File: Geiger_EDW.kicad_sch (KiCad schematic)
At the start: 44 parts, among them J1 Power, J2 +5V Output, J3 STS-5, J4 Piezo, J5 Output, P1 500k, Q1 IRF7404, Q2 BC857, Q3 IRFBC40SPBF, Q4 BC847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

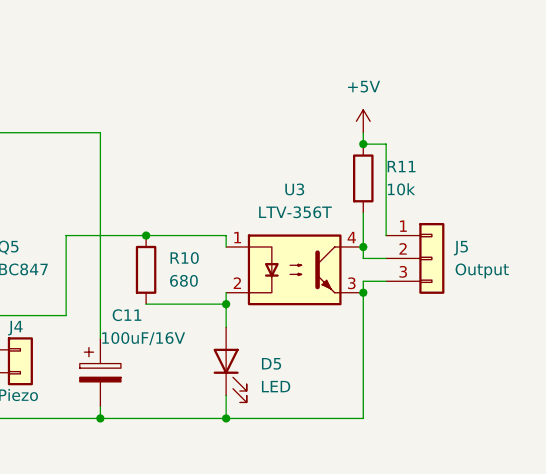
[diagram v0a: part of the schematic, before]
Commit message: Change R11 value from 10k to 1k
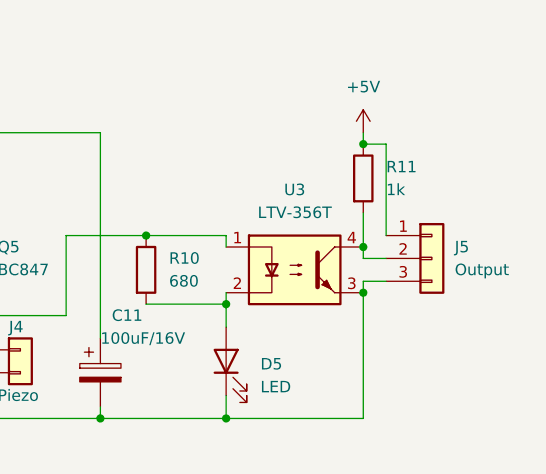
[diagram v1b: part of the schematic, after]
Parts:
- R11: value 10k -> 1k
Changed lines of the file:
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@@
       (effects (font (size 1.27 1.27)) (justify left))
     )
-    (property "Value" "10k" (at 219.71 31.75 0)
+    (property "Value" "1k" (at 219.71 31.75 0)
       (effects (font (size 1.27 1.27)) (justify left))
     )
